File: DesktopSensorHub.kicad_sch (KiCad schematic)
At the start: 44 parts, among them J1 USB_C_Receptacle_USB2.0, SW1 TS02-66-50-BK-160-LCR-D, U1 RP2040, U2 APDS-9960, U3 AP2112K-3.3, U5 W25Q32JVSS, Y1 12 MHZ

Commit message: varius small changes to approach a layout
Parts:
- C11, C21: footprint Capacitor_SMD:C_0603_1608Metric -> Capacitor_SMD:C_0402_1005Metric
- J1: footprint Connector_USB:USB_C_Receptacle_Molex_105450-0101 -> Connector_USB:USB_C_Receptacle_GCT_USB4105-xx-A_16P_TopMnt_Horizontal; MPN (none) -> USB4105-GF-A
- JMP1: renamed from R4; footprint Resistor_SMD:R_0805_2012Metric_Pad1.20x1.40mm_HandSolder -> Jumper:SolderJumper-2_P1.3mm_Open_TrianglePad1.0x1.5mm
- U5: footprint Package_SO:SOIC-8_5.23x5.23mm_P1.27mm -> Package_SO:SOIC-8_5.275x5.275mm_P1.27mm
- renumbered RUSB1 to R11, RUSB2 to R12
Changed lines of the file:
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@@
   (symbol (lib_id "Device:R") (at 229.87 39.37 90) (unit 1)
     (in_bom yes) (on_board yes) (dnp no)
-    (property "Reference" "RUSB2" (at 229.87 41.91 90)
+    (property "Reference" "R12" (at 229.87 41.91 90)
       (effects (font (size 1.27 1.27)))
     )
@@
       (project "DesktopSensorHub"
         (path "/48c0c7ef-0fb2-4c47-a984-821bb99e66ea"
-          (reference "RUSB2") (unit 1)
+          (reference "R12") (unit 1)
         )
       )
@@
       (effects (font (size 1.27 1.27)) (justify left))
     )
-    (property "Footprint" "Capacitor_SMD:C_0603_1608Metric" (at 69.5452 72.39 0)
+    (property "Footprint" "Capacitor_SMD:C_0402_1005Metric" (at 69.5452 72.39 0)
       (effects (font (size 1.27 1.27)) hide)
     )
@@
   (symbol (lib_id "Device:R") (at 205.74 69.85 90) (unit 1)
     (in_bom yes) (on_board yes) (dnp yes)
-    (property "Reference" "R4" (at 205.74 72.39 90)
+    (property "Reference" "JMP1" (at 205.74 72.39 90)
       (effects (font (size 1.27 1.27)))
     )
@@
       (effects (font (size 1.27 1.27)))
     )
-    (property "Footprint" "Resistor_SMD:R_0805_2012Metric_Pad1.20x1.40mm_HandSolder" (at 205.74 71.628 90)
+    (property "Footprint" "Jumper:SolderJumper-2_P1.3mm_Open_TrianglePad1.0x1.5mm" (at 205.74 71.628 90)
       (effects (font (size 1.27 1.27)) hide)
     )
@@
       (project "DesktopSensorHub"
         (path "/48c0c7ef-0fb2-4c47-a984-821bb99e66ea"
-          (reference "R4") (unit 1)
+          (reference "JMP1") (unit 1)
         )
       )
@@
       (effects (font (size 1.27 1.27)))
     )
-    (property "Footprint" "Connector_USB:USB_C_Receptacle_Molex_105450-0101" (at 213.36 46.99 0)
-      (effects (font (size 1.27 1.27)) hide)
-    )
-    (property "Datasheet" "https://www.usb.org/sites/default/files/documents/usb_type-c.zip" (at 213.36 46.99 0)
+    (property "Footprint" "Connector_USB:USB_C_Receptacle_GCT_USB4105-xx-A_16P_TopMnt_Horizontal" (at 213.36 46.99 0)
+      (effects (font (size 1.27 1.27)) hide)
+    )
+    (property "Datasheet" "https://media.digikey.com/pdf/Data%20Sheets/GCT%20PDFs/USB4105%20-%20Product%20Drawing.pdf" (at 213.36 46.99 0)
+      (effects (font (size 1.27 1.27)) hide)
+    )
+    (property "MPN" "USB4105-GF-A" (at 209.55 46.99 0)
       (effects (font (size 1.27 1.27)) hide)
     )
@@
       (effects (font (size 1.27 1.27)) (justify left))
     )
-    (property "Footprint" "Capacitor_SMD:C_0603_1608Metric" (at 105.1052 72.39 0)
+    (property "Footprint" "Capacitor_SMD:C_0402_1005Metric" (at 105.1052 72.39 0)
       (effects (font (size 1.27 1.27)) hide)
     )
@@
       (effects (font (size 1.27 1.27)) (justify left))
     )
-    (property "Footprint" "Package_SO:SOIC-8_5.23x5.23mm_P1.27mm" (at 34.29 116.84 0)
+    (property "Footprint" "Package_SO:SOIC-8_5.275x5.275mm_P1.27mm" (at 34.29 116.84 0)
       (effects (font (size 1.27 1.27)) hide)
     )
@@
   (symbol (lib_id "Device:R") (at 229.87 36.83 90) (unit 1)
     (in_bom yes) (on_board yes) (dnp no)
-    (property "Reference" "RUSB1" (at 229.87 34.29 90)
+    (property "Reference" "R11" (at 229.87 34.29 90)
       (effects (font (size 1.27 1.27)))
     )
@@
       (project "DesktopSensorHub"
         (path "/48c0c7ef-0fb2-4c47-a984-821bb99e66ea"
-          (reference "RUSB1") (unit 1)
-        )
-      )
+          (reference "R11") (unit 1)
+        )
+      )

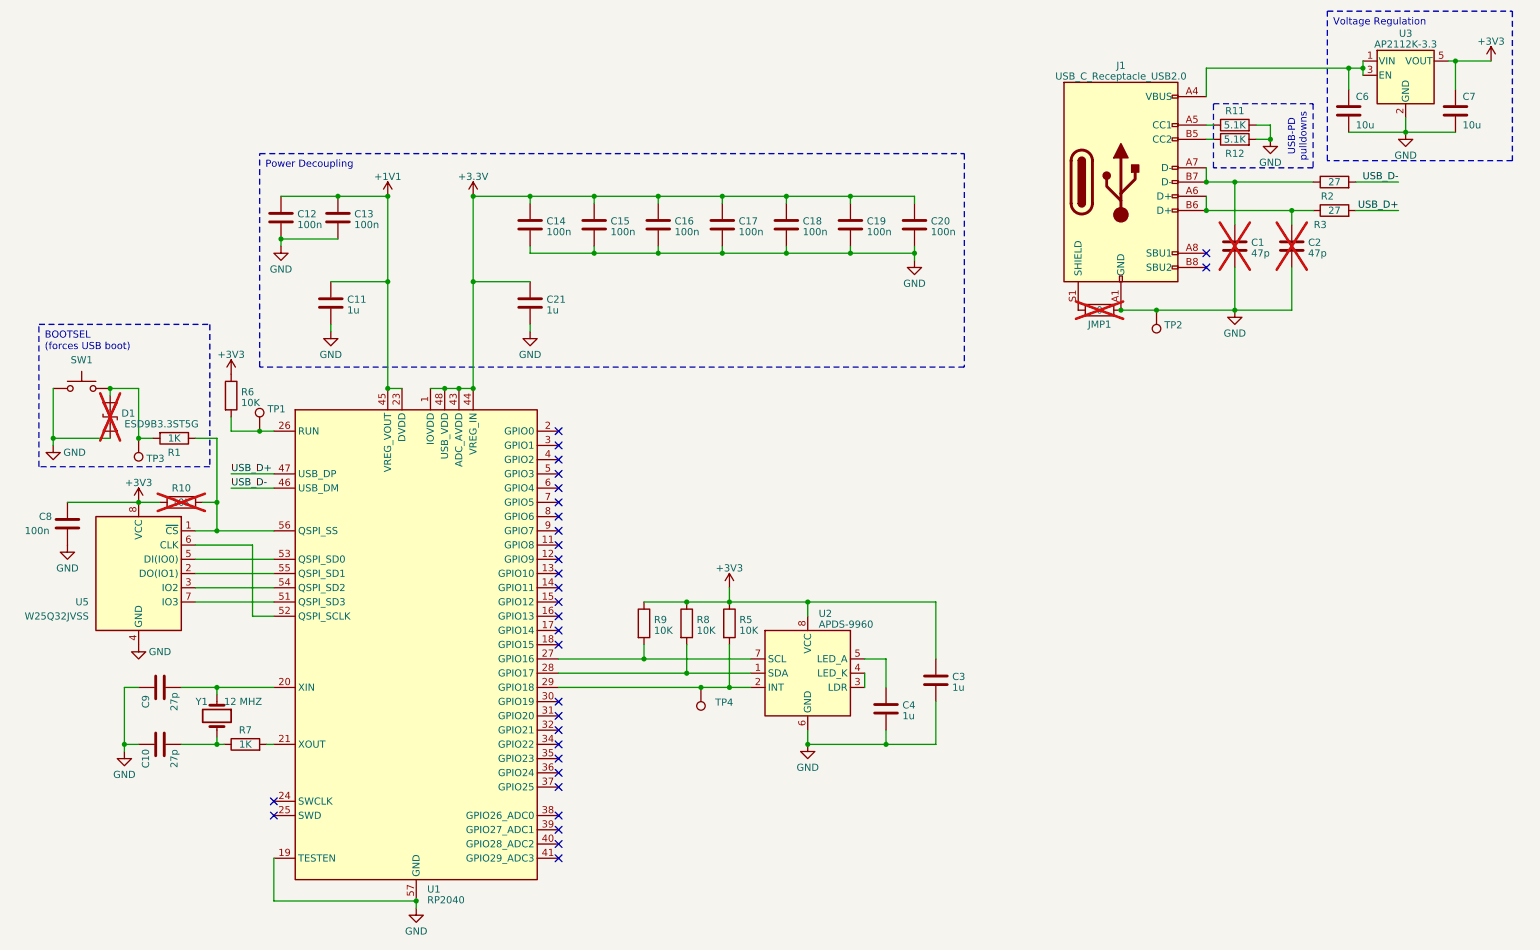
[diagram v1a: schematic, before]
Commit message: finish layout, include design files sent to OSHPark
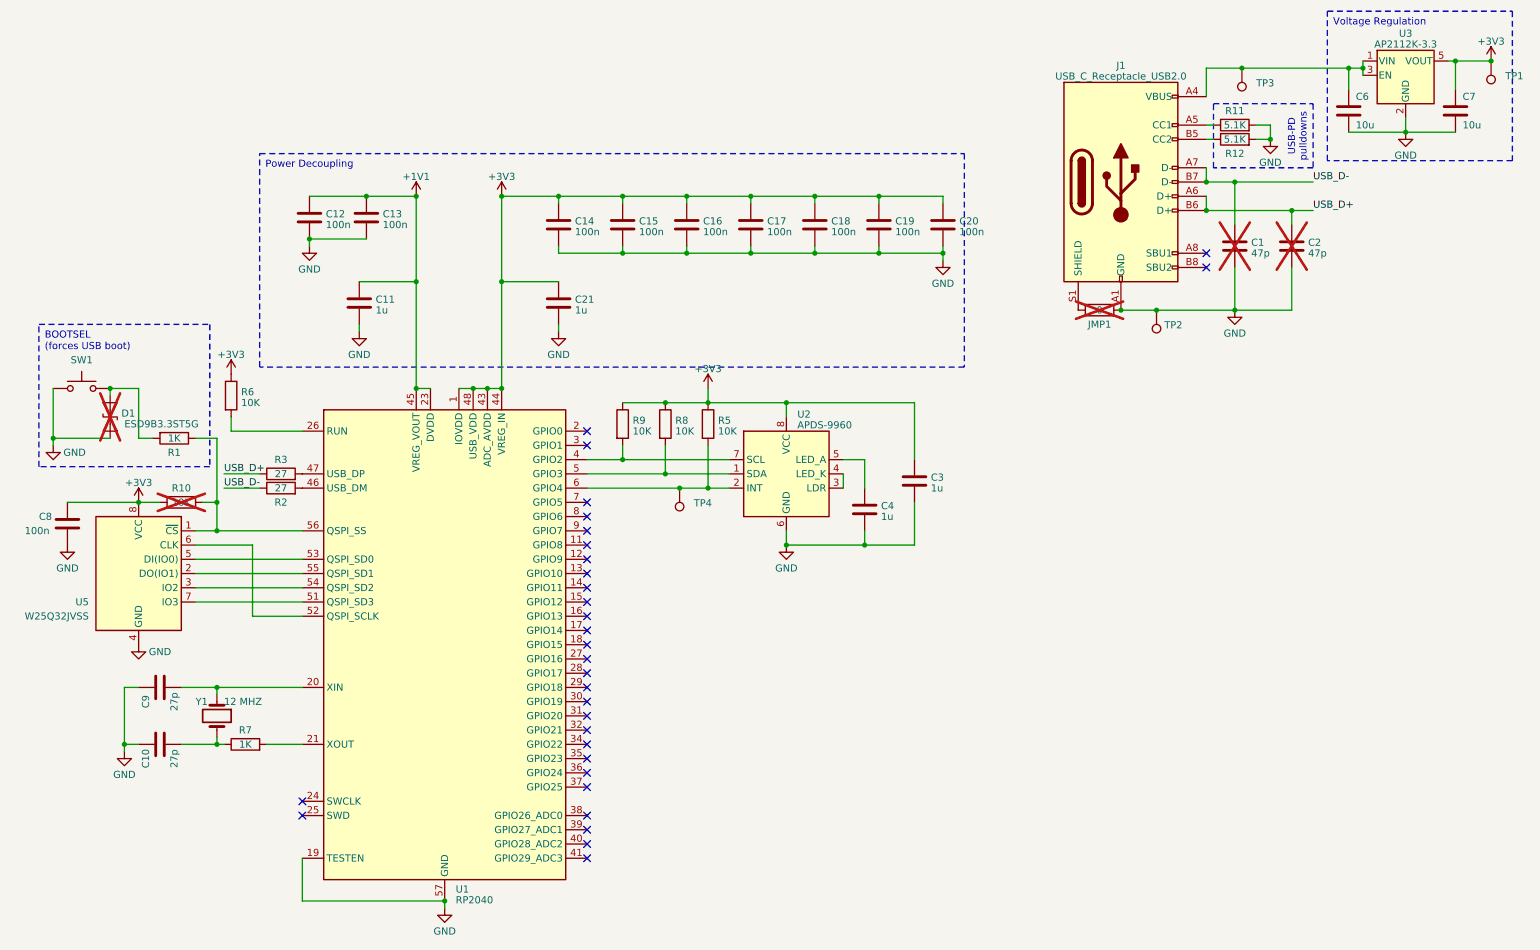
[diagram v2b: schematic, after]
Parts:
- C1, C2, C3, C4: footprint Capacitor_SMD:C_0603_1608Metric -> Capacitor_SMD:C_0402_1005Metric
- C10, C9: footprint Capacitor_SMD:C_1206_3216Metric -> Capacitor_SMD:C_0402_1005Metric
- C12, C13, C14, C15, C16, C17, C18, C19, C20, C8: footprint Capacitor_SMD:C_0201_0603Metric -> Capacitor_SMD:C_0402_1005Metric
- C6, C7: footprint Capacitor_SMD:C_0201_0603Metric -> Capacitor_SMD:C_0805_2012Metric
- R10, R5, R6, R8, R9: footprint Resistor_SMD:R_0805_2012Metric -> Resistor_SMD:R_0402_1005Metric
- TP1, TP2, TP3, TP4: footprint TestPoint:TestPoint_Pad_D2.0mm -> TestPoint:TestPoint_Pad_D1.5mm
- U1: footprint Package_DFN_QFN:QFN-56-1EP_7x7mm_P0.4mm_EP3.2x3.2mm -> DesktopSensorHub footprints:RP2040-QFN-56
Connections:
- net +3.3V is gone; now on net +3V3: C14.1, C15.1, C16.1, C17.1, C18.1, C19.1, C20.1, C21.1, U1.1 (IOVDD), U1.10 (IOVDD), U1.22 (IOVDD), U1.33 (IOVDD), U1.42 (IOVDD), U1.43 (ADC_AVDD), U1.44 (VREG_IN), U1.48 (USB_VDD), U1.49 (IOVDD)
- net +3V3: now also TP1.1
- net USB_D+: now also C2.1, J1.A6 (D+), J1.B6 (D+), R3.1; no longer R3.2, U1.47 (USB_DP)
- net USB_D-: now also C1.1, J1.A7 (D-), J1.B7 (D-), R2.1; no longer R2.2, U1.46 (USB_DM)
- net at C6.1, J1.A4 (VBUS), J1.A9 (VBUS)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: now also TP3.1
- net at R6.2, U1.26 (RUN): no longer TP1.1
- net at R9.2, U2.7 (SCL): now also U1.4 (GPIO2); no longer U1.27 (GPIO16)
- net at R8.2, U2.1 (SDA): now also U1.5 (GPIO3); no longer U1.28 (GPIO17)
- net at R5.2, TP4.1, U2.2 (INT): now also U1.6 (GPIO4); no longer U1.29 (GPIO18)
- net at D1.1 (A1), R1.2, SW1.2: no longer TP3.1
- new net: R2.2, U1.46 (USB_DM)
- new net: R3.2, U1.47 (USB_DP)
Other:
- moved on the sheet: C11, C12, C13, C14, C15, C16, C17, C18, C19, C20, C21, C3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
